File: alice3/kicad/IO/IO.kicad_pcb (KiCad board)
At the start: 2 copper layers, 22 parts, among them CON1 SD_Card, U1 MiniM4-D40, U2 LEVELCONVERTER, U3 LEVELCONVERTER, U4 LEVELCONVERTER, U5 LEVELCONVERTER, U6 Alice_3_bus, U7 DFROBOT_FTDI_BASIC, U8 LM2937-3.3, X1 MINI_DIN_6

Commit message: IO board PCB
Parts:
- moved U7 149.0 mm to (177.8, 69.8), turned to 180 degrees
- moved X1 137.7 mm to (172.7, 137.2), turned to 90 degrees
- moved C2 95.1 mm to (102.9, 116.8), turned to 270 degrees
- moved R3 94.0 mm to (167.6, 94.0), turned to 180 degrees
- moved CON1 92.7 mm to (143.5, 111.8)
- moved U6 91.4 mm to (114.3, 100.3), turned to 0 degrees
- moved U8 81.5 mm to (101.6, 106.7), turned to 0 degrees
- moved U1 77.6 mm to (156.2, 129.5), turned to 270 degrees
- moved R0 77.5 mm to (139.7, 119.4), turned to 90 degrees
- moved PANIC1 72.5 mm to (99.1, 72.4)
- moved R2 72.4 mm to (152.4, 94.0), turned to 180 degrees
- moved R1 71.8 mm to (139.7, 104.1), turned to 270 degrees
- moved C1 68.2 mm to (151.1, 87.6), turned to 90 degrees
- moved INFO1 65.0 mm to (99.1, 81.3)
- moved R5 60.1 mm to (116.8, 74.9), turned to 0 degrees
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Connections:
- U2 pad 11: /D1 -> /D1.5v
- U2 pad 12: /D0 -> /D0.5v
- U2 pad 7: /D3 -> /D3.5v
- U2 pad 8: /D2 -> /D2.5v
- U3 pad 11: /D5 -> /D5.5v
- U3 pad 12: /D4 -> /D4.5v
- U3 pad 7: /D7 -> /D7.5v
- U3 pad 8: /D6 -> /D6.5v
- U4 pad 11: //RD -> //RD.5v
- U4 pad 12: //IORQ -> //IORQ.5v
- U4 pad 7: /A7 -> /A7.5v
- U4 pad 8: //WR -> //WR.5v
- U5 pad 11: //RESET -> //RESET.5v
- U5 pad 12: //INT -> //INT.5v
- U5 pad 7: //M1 -> //M1.5v
- U5 pad 8: //WAIT -> //WAIT.5v
- U6 pad 11: /D0 -> /D0.5v
- U6 pad 12: /D1 -> /D1.5v
- U6 pad 13: /D2 -> /D2.5v
- U6 pad 14: /D3 -> /D3.5v
- U6 pad 15: /D4 -> /D4.5v
- U6 pad 16: /D5 -> /D5.5v
- U6 pad 17: /D6 -> /D6.5v
- U6 pad 18: /D7 -> /D7.5v
- U6 pad 19: /A7 -> /A7.5v
- U6 pad 3: //INT -> //INT.5v
- U6 pad 4: //RESET -> //RESET.5v
- U6 pad 5: //WAIT -> //WAIT.5v
- U6 pad 6: //M1 -> //M1.5v
- U6 pad 7: //RD -> //RD.5v
- U6 pad 8: //WR -> //WR.5v
- U6 pad 9: //IORQ -> //IORQ.5v
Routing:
- net GND: track 0.00 -> 286.5 mm, vias 0 -> 1
- net +3V3: track 0.00 -> 209.4 mm
- net +5V: track 0.00 -> 144.9 mm
- net Net-(U1-Pad25): track 0.00 -> 108.2 mm
- net Net-(U1-Pad26): track 0.00 -> 95.7 mm
- net /DO: track 0.00 -> 85.6 mm, vias 0 -> 2
- net //M1: track 0.00 -> 79.3 mm, vias 0 -> 1
- net Net-(HEART1-Pad2): track 0.00 -> 74.4 mm
- net Net-(PANIC1-Pad2): track 0.00 -> 69.0 mm
- net //WAIT: track 0.00 -> 64.6 mm
- net /SCK: track 0.00 -> 63.1 mm
- net /DI: track 0.00 -> 62.1 mm
- net Net-(INFO1-Pad2): track 0.00 -> 61.0 mm
- net //INT: track 0.00 -> 59.9 mm
- net /D3: track 0.00 -> 54.5 mm
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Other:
- board outline added: 87.6 x 81.3 mm
- net class OSHPark added: clearance 0.1524, trace_width 0.1524, via_dia 0.635, via_drill 0.3302
- rule trace_min: 0.2 -> 0.1524
- board text added: "Alice 3 IO Earwig, Inc grantham@plunk.org"
- board text added: "Mini-M4"

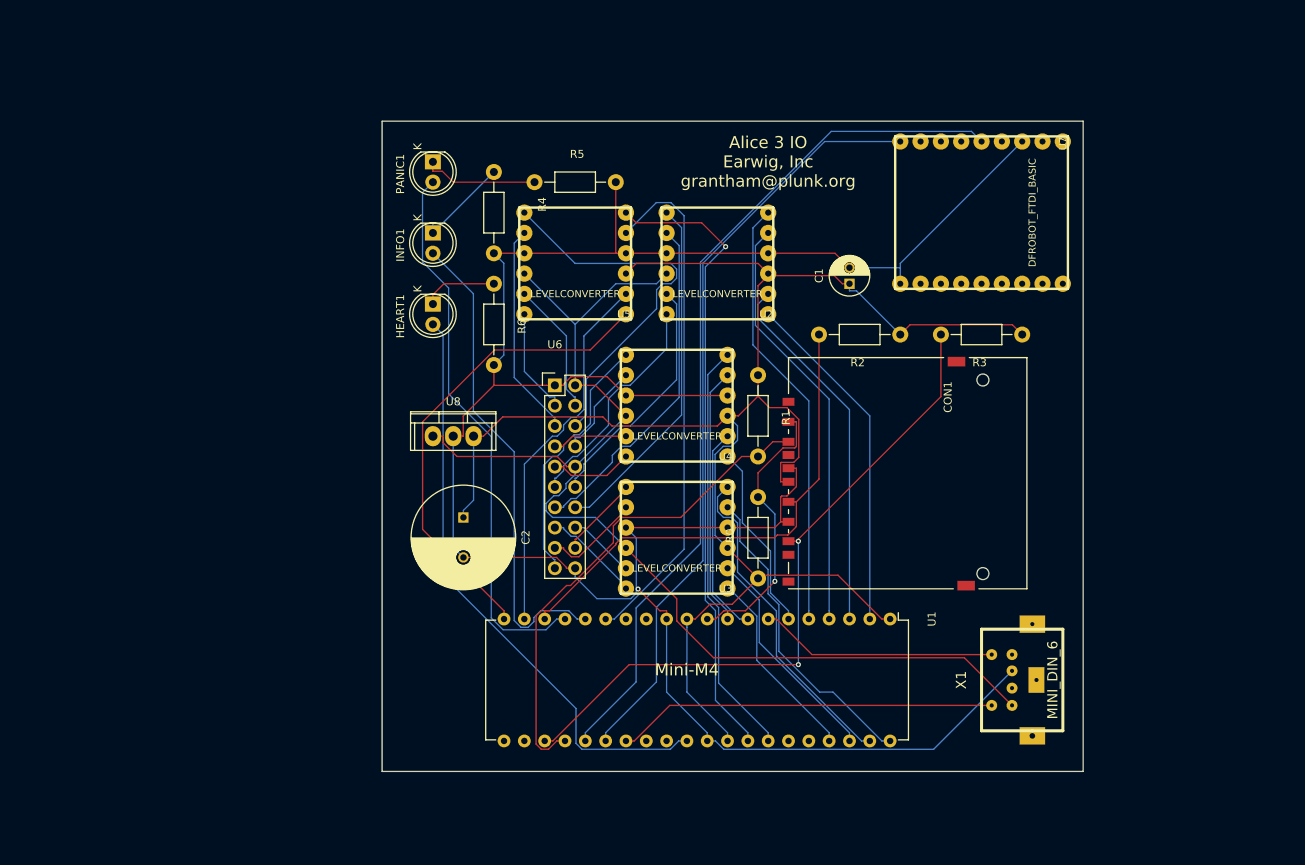
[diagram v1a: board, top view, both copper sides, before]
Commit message: tighter PDB, copper fill
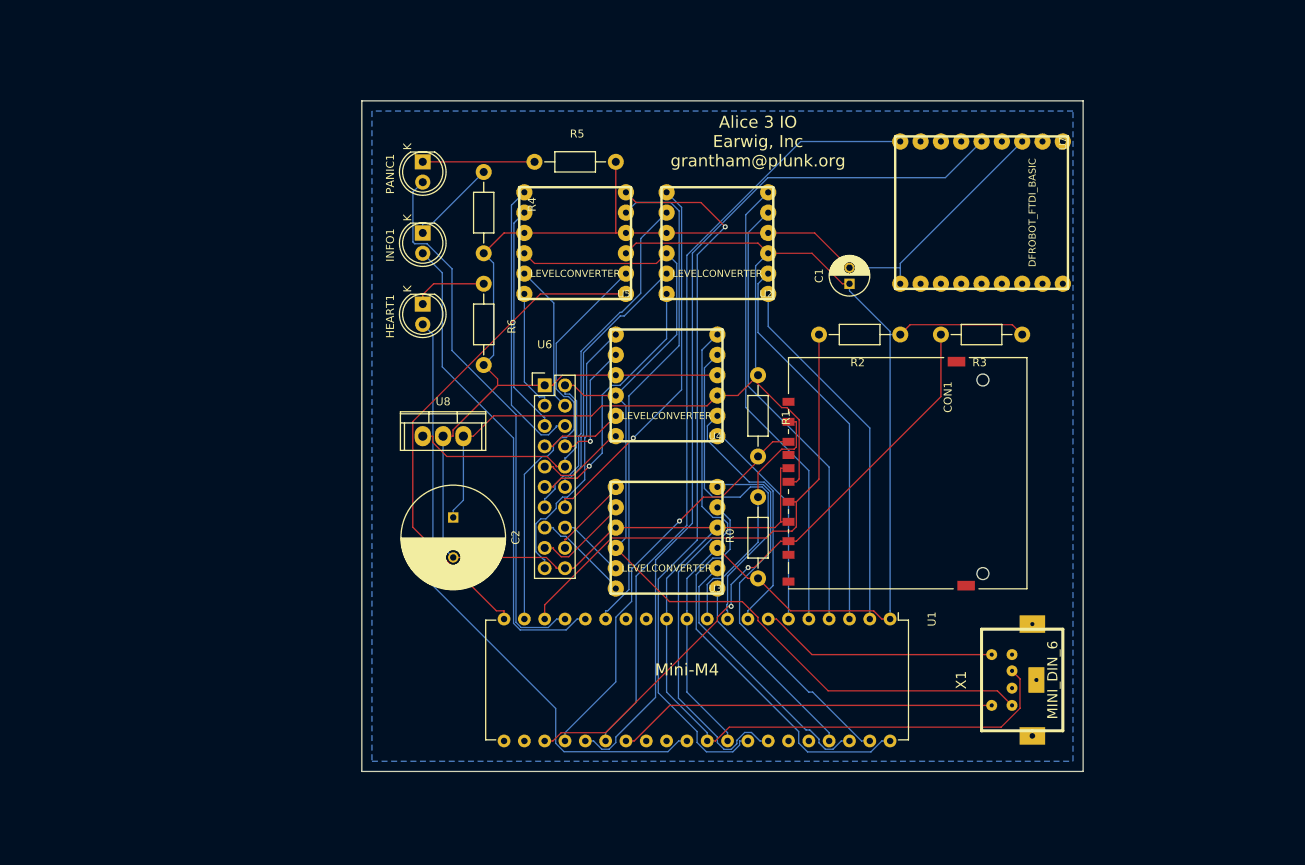
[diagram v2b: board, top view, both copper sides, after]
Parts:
- moved U4 2.84 mm to (134.6, 106.7)
- moved R5 2.54 mm to (116.8, 72.4)
- moved U2 2.54 mm to (141.0, 88.9)
- moved U5 2.54 mm to (123.2, 88.9)
- moved C2 1.27 mm to (101.6, 116.8)
- moved R4 1.27 mm to (105.4, 78.7)
- moved R6 1.27 mm to (105.4, 92.7)
- moved HEART1 1.27 mm to (97.8, 90.2)
- moved INFO1 1.27 mm to (97.8, 81.3)
- moved PANIC1 1.27 mm to (97.8, 72.4)
- moved U6 1.27 mm to (113.0, 100.3)
- moved U8 1.27 mm to (100.3, 106.7)
- moved U3 1.27 mm to (134.6, 125.7)
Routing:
- net +3V3: track 209.4 -> 228.5 mm
- net /A7: track 52.4 -> 67.2 mm
- net //M1: track 79.3 -> 91.8 mm
- net //WR: track 32.3 -> 44.6 mm
- net +5V: track 144.9 -> 156.9 mm
- net //M1.5v: track 47.4 -> 36.0 mm
- net /D6: track 39.2 -> 50.3 mm
- net /DI: track 62.1 -> 51.5 mm, vias 0 -> 1
- net /DO: track 85.6 -> 77.0 mm
- net /D7: track 41.4 -> 47.5 mm
- net /D5: track 27.9 -> 33.9 mm
- net //RD: track 26.1 -> 31.7 mm
- net //RESET: track 46.6 -> 51.4 mm
- net /D0.5v: track 28.4 -> 32.9 mm, vias 0 -> 1
- net //WR.5v: track 11.9 -> 15.6 mm, vias 0 -> 1
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- added copper zone on B.Cu, net GND
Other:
- board size 87.6 x 81.3 mm -> 90.2 x 83.8 mm
